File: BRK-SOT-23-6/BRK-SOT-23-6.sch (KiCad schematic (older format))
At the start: 3 parts, among them J1 Conn_01x03, J2 Conn_01x03, U1 SC-70-6

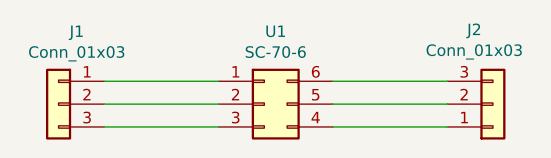
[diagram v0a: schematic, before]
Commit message: BRK-SOT-23-6, BSK-MSOP-8-3x3-P0.65, BRK-VSSOP-8-2.4x2.1-P0.5
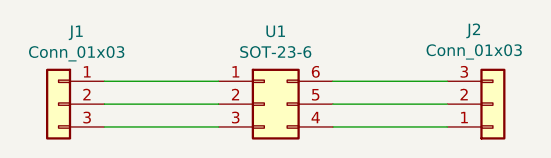
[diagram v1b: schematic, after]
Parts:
- U1: value SC-70-6 -> SOT-23-6; footprint Package_TO_SOT_SMD:SOT-363_SC-70-6_Handsoldering -> Package_TO_SOT_SMD:SOT-23-6_Handsoldering
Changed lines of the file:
@@
 EESchema Schematic File Version 4
-LIBS:BRK-SC-70-6-cache
+LIBS:BRK-SOT-23-6-cache
 EELAYER 26 0
 EELAYER END
@@
 encoding utf-8
 Sheet 1 1
-Title "BRK-SC-70-6"
+Title "BRK-SOT-23-6"
 Date ""
 Rev "v1.0"
@@
 P 5700 3900
 F 0 "U1" H 5750 4217 50  0000 C CNN
-F 1 "SC-70-6" H 5750 4126 50  0000 C CNN
-F 2 "Package_TO_SOT_SMD:SOT-363_SC-70-6_Handsoldering" H 5700 3900 50  0001 C CNN
+F 1 "SOT-23-6" H 5750 4126 50  0000 C CNN
+F 2 "Package_TO_SOT_SMD:SOT-23-6_Handsoldering" H 5700 3900 50  0001 C CNN
 F 3 "~" H 5700 3900 50  0001 C CNN
 	1    5700 3900
